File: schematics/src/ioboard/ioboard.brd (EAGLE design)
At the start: 53.3 x 33.7 mm, 16 parts

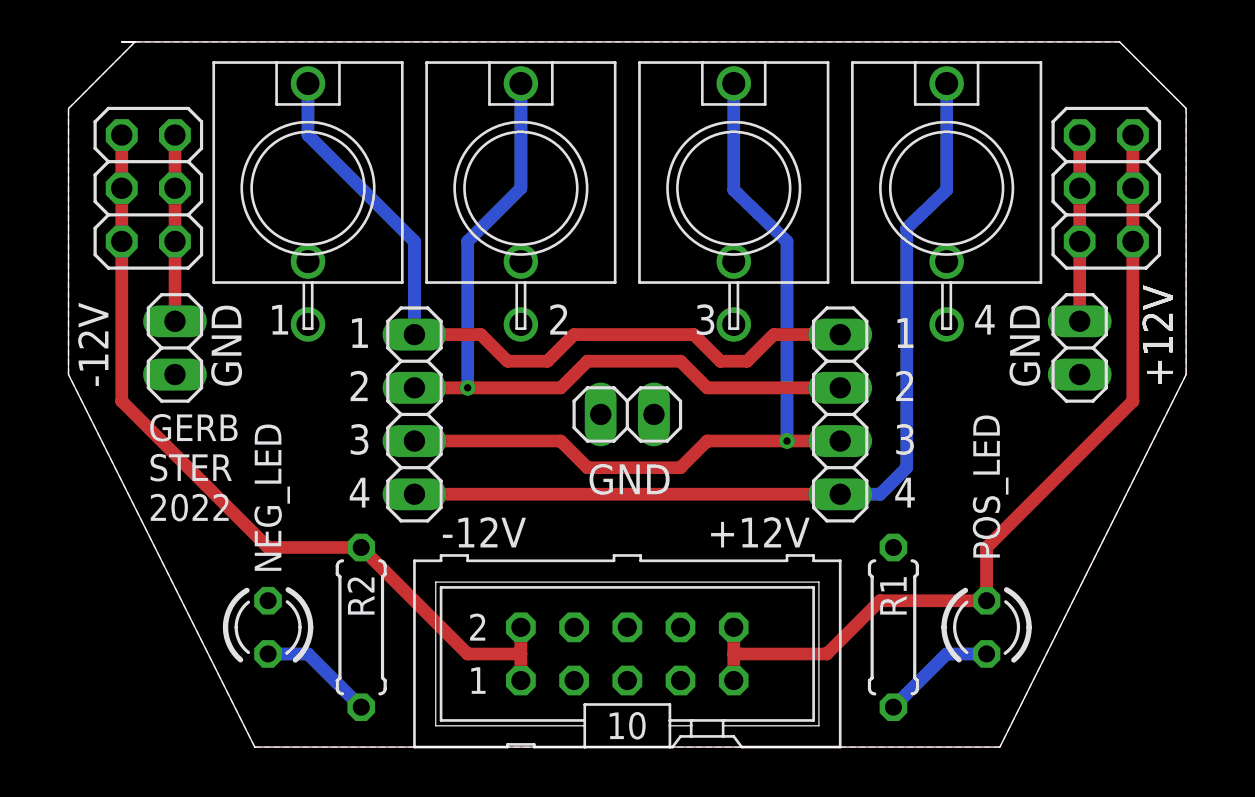
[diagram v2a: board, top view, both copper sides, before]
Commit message: Fixed schematics
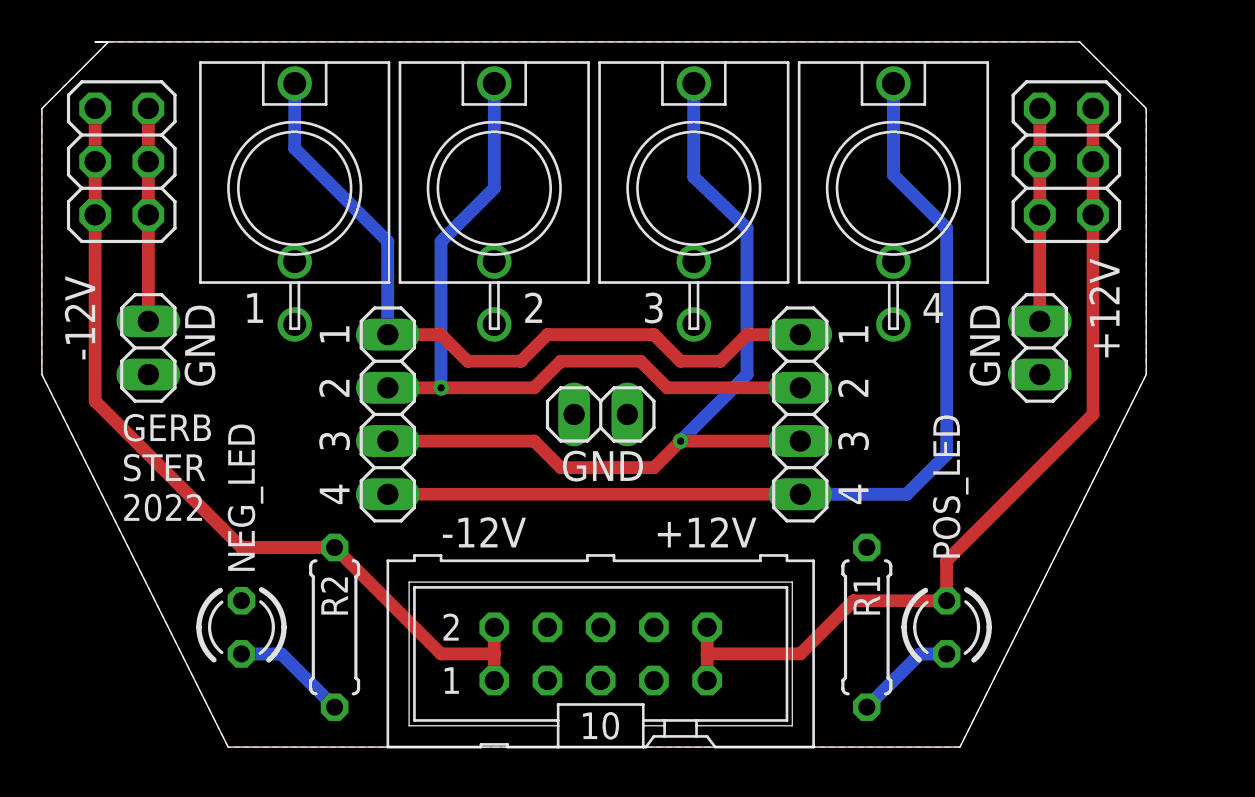
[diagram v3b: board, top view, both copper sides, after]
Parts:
- moved JACK5 2.54 mm to (40.6, 26.7)
- moved JP1 2.29 mm to (48.9, 27.9)
- moved JACK3 1.91 mm to (31.1, 26.7)
- moved JP5 1.91 mm to (36.2, 15.9)
- moved JP6 1.91 mm to (47.6, 19.1)
- moved POS_LED 1.91 mm to (43.2, 5.71)
- moved JP3 1.80 mm to (3.81, 27.9)
- moved R1 1.27 mm to (39.4, 5.71)
- moved GND_JMP 1.27 mm to (5.08, 19.1)
- moved JACK2 1.27 mm to (21.6, 26.7)
- moved JP8 1.27 mm to (16.5, 15.9)
- moved JP9 1.27 mm to (26.7, 15.9)
- moved NEG_LED 1.27 mm to (9.53, 5.71)
- moved PWR 1.27 mm to (26.7, 4.45)
- moved R2 1.27 mm to (14.0, 5.71)
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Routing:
- net N$7: track 43.2 -> 46.2 mm
- net N$9: track 8.89 -> 10.2 mm
- net N$6: track 8.89 -> 10.2 mm
- net -12V: track 39.3 -> 40.6 mm
- net N$3: track 36.5 -> 35.6 mm
- net N$5: track 39.5 -> 40.2 mm
- net N$10: track 36.9 -> 36.3 mm
- net N$1: track 5.50 -> 4.86 mm
- net +12V: track 40.8 -> 41.4 mm
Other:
- board size 53.3 x 33.7 mm -> 52.7 x 33.7 mm
